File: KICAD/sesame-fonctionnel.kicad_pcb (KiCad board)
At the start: 4 copper layers, 160 x 100 mm, 279 parts, among them J1 CXS70-14-C, J2 CXS70-14-C, J7 CXS70-14-C, J8 CXS70-14-C, J9 Conn_02x16_Odd_Even, Q1 BC847, Q10 BC857, Q11 SQM120, Q12 BC847, Q13 BC847, Q2 BC847, Q3 BC847, Q4 BC847, Q5 BC847, Q6 SQM120, Q7 BC857, Q8 SQM120, Q9 SQM120, U1 AD8030, U10 LT6016, U11 AD8030, U12 UCC27284-Q1, U13 AD8030, U14 AD8030, U15 LT8365, U16 LM4040DBZ-2.5, U17 UCC27284-Q1, U2 LM2903, U3 CD4053BM96, U4 4011, U5 CD4053BM96, U6 CD4053BM96, U7 AD8030, U8 LT6016, U9 AD8030

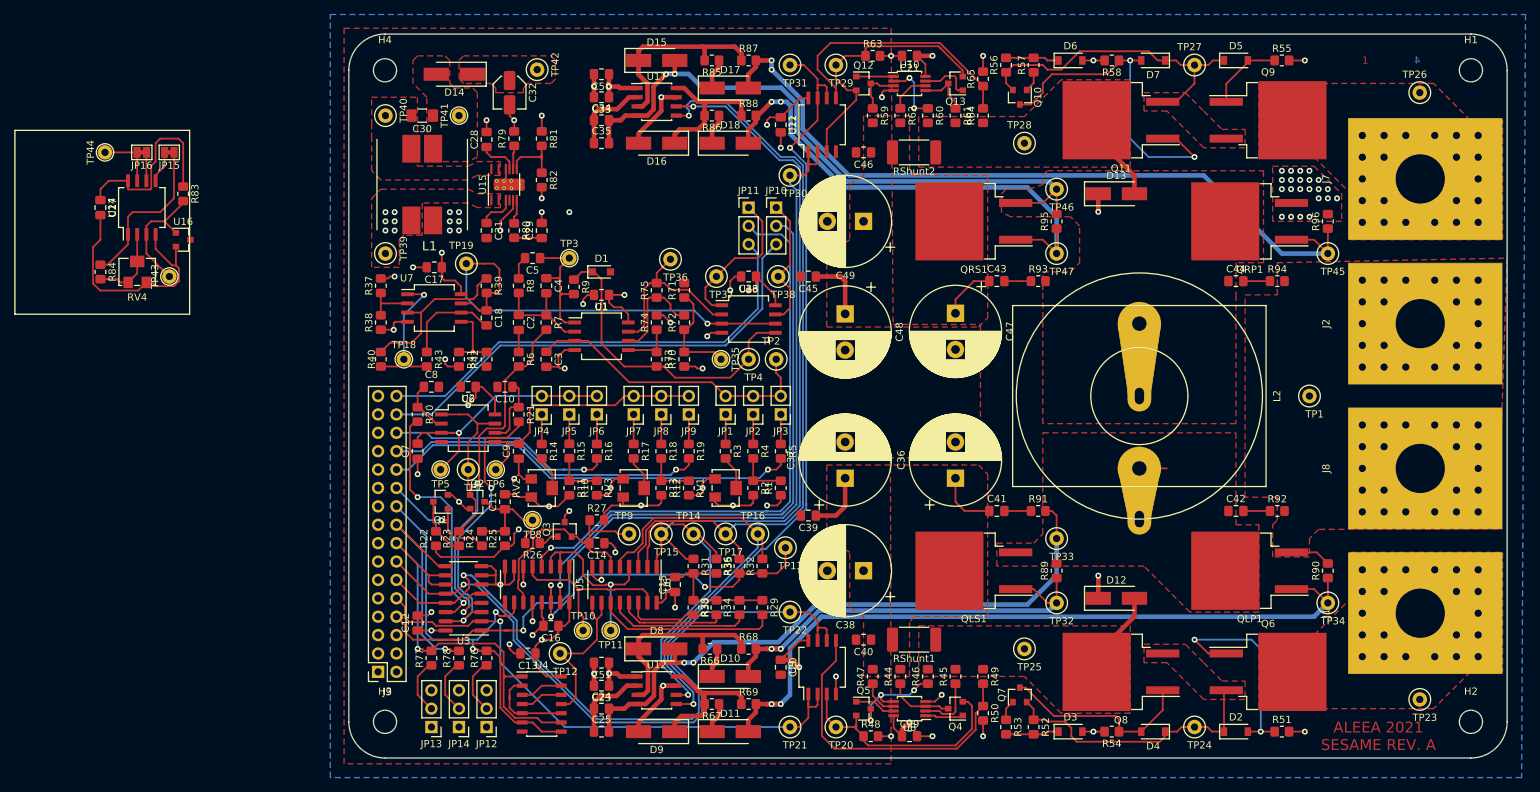
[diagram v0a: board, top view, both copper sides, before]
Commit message: changed ground planes
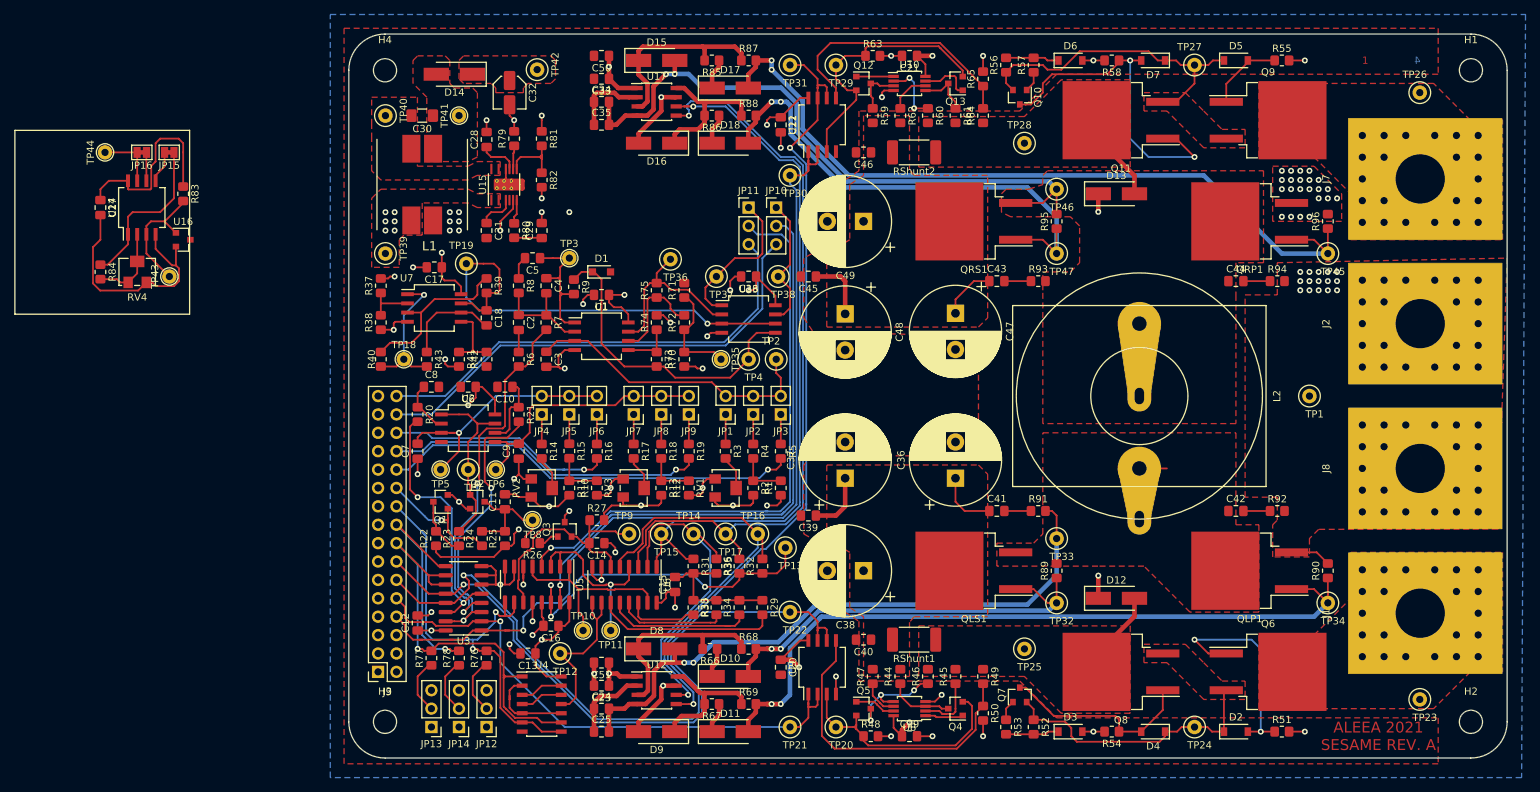
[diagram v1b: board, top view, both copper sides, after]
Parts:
- moved C34 2.54 mm to (114.9, 69.4)
- moved C35 2.54 mm to (114.9, 72.5)
- moved C50 2.54 mm to (114.9, 63.0)
- moved C33 2.54 mm to (114.9, 66.2)
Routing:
- net (no net): track 8.89 -> 0.00 mm
- net GND: track 226.0 -> 222.8 mm, vias 66 -> 80
- net Net-(C34-Pad1): track 11.0 -> 10.4 mm
- added copper zone on In1.Cu, net GND
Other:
- board text added: "Driver Command"

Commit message: enhanced copper planes
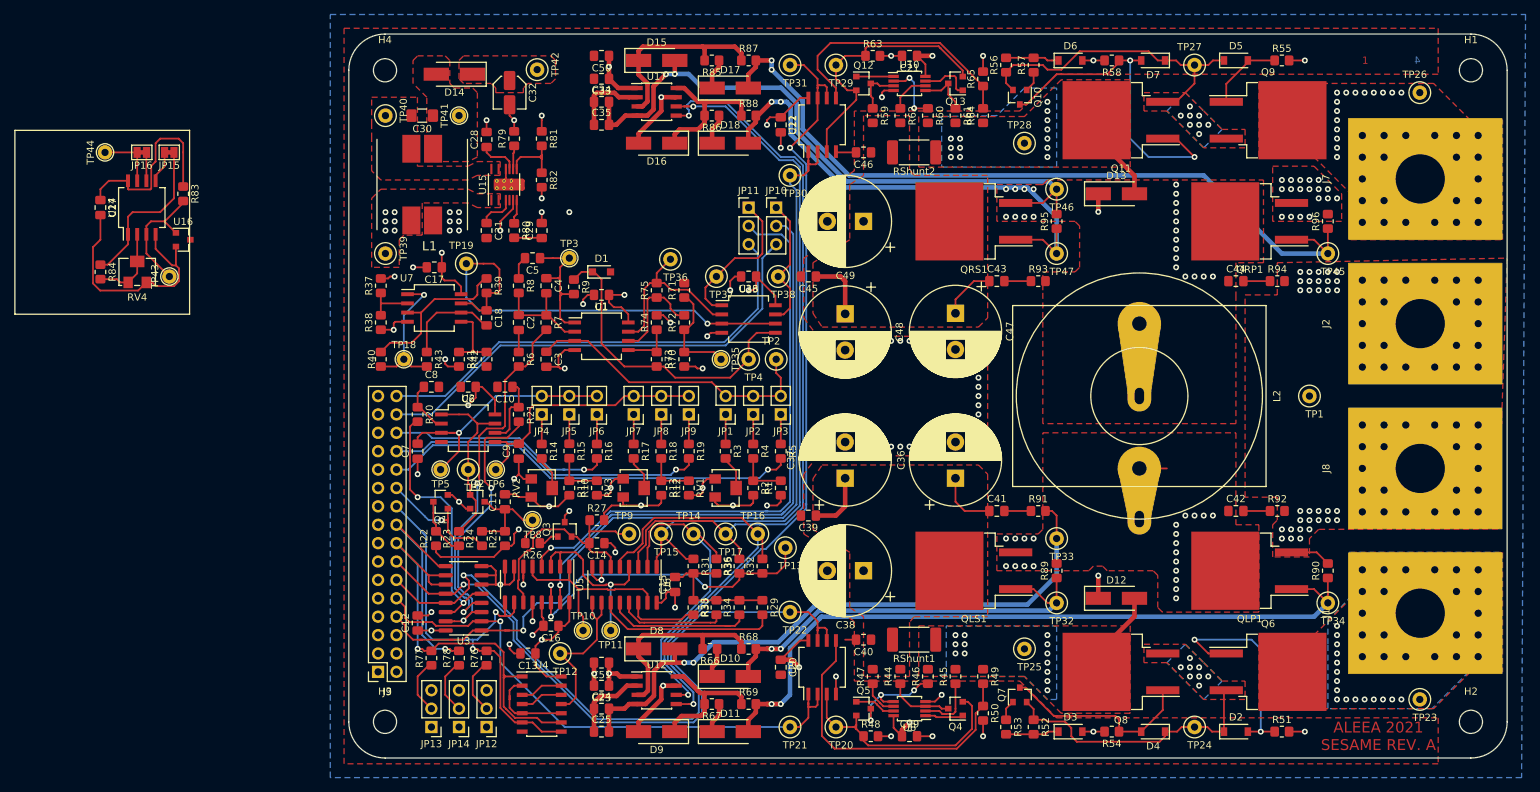
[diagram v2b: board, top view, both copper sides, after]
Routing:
- net GND: track 222.8 -> 227.1 mm, vias 80 -> 122
- net Net-(D7-Pad2): track 46.4 -> 45.6 mm
- net Net-(D5-Pad1): vias 0 -> 8
- net Net-(D2-Pad1): vias 0 -> 8
- net /VProt_Right: vias 0 -> 13
- net /VProt_Left: vias 0 -> 13
- net /R: vias 0 -> 15
- net /MOS DRIVER R/VS: vias 2 -> 21
- net /MOS DRIVER R/VG_P: vias 2 -> 5
- net /MOS DRIVER L/VS: vias 2 -> 23
- net /L: vias 0 -> 16
- added copper zone on B.Cu, net /L
- added copper zone on B.Cu, net /VProt_Left
- added copper zone on B.Cu, net /VProt_Right
- added copper zone on B.Cu, net Net-(D2-Pad1)
- added copper zone on B.Cu, net Net-(D5-Pad1)

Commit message: 0 conn. + new vref
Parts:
- removed JP15, JP16: Jumper_2_Bridged, Jumper:SolderJumper-2_P1.3mm_Bridged_Pad1.0x1.5mm
- removed RV4: 10K, Potentiometer_SMD:Potentiometer_Bourns_3214W_Vertical
- removed TP43, TP44: TP_NOP, TestPoint:TestPoint_THTPad_D2.0mm_Drill1.0mm
- removed U14: AD8030, Package_SO:SO-8_5.3x6.2mm_P1.27mm
- added R28: R, Sesame_footprint:R_0805_2012Metric_Pad1.20x1.40mm_HandSolder, F.Cu at (120.0, 80.2)
- R84: value 10k -> R
- U16: value LM4040DBZ-2.5 -> TL431DBZ
- moved R84 74.7 mm to (120.0, 85.2)
- moved C27 68.1 mm to (113.6, 80.2)
- moved U16 67.6 mm to (124.4, 82.7)
- moved R83 59.7 mm to (116.8, 80.2), turned to 90 degrees
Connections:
- C27 pad 1: VCC -> VREF
- R83 pad 2: Net-(R83-Pad2) -> VREF
- R84 pad 1: VREF -> Net-(R28-Pad2)
- R84 pad 2: Net-(R84-Pad2) -> GND
- U16 pad 1: Net-(R83-Pad2) -> VREF
- U16 pad 2: GND -> Net-(R28-Pad2)
- U16 pad 3: (no net) -> GND
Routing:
- net VCC: track 154.6 -> 129.1 mm, vias 19 -> 20
- net VREF: track 280.7 -> 297.6 mm
- net Net-(R83-Pad2): track 16.3 -> 0.00 mm
- net GND: track 227.1 -> 211.3 mm, vias 122 -> 123
- net Net-(R84-Pad2): track 11.2 -> 0.00 mm
- net Net-(JP16-Pad2): track 8.36 -> 0.00 mm
- net Net-(R28-Pad2): track 0.00 -> 6.77 mm
- net Net-(JP15-Pad2): track 4.43 -> 0.00 mm
- net Net-(JP16-Pad1): track 3.93 -> 0.00 mm
- net /MOS DRIVER R/VS: vias 21 -> 20
- net /MOS DRIVER R/VG_P: vias 5 -> 2

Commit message: mod. ref rail on kicad
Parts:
- R28: value R -> 14k
- R83: value R -> 200
- R84: value R -> 10k

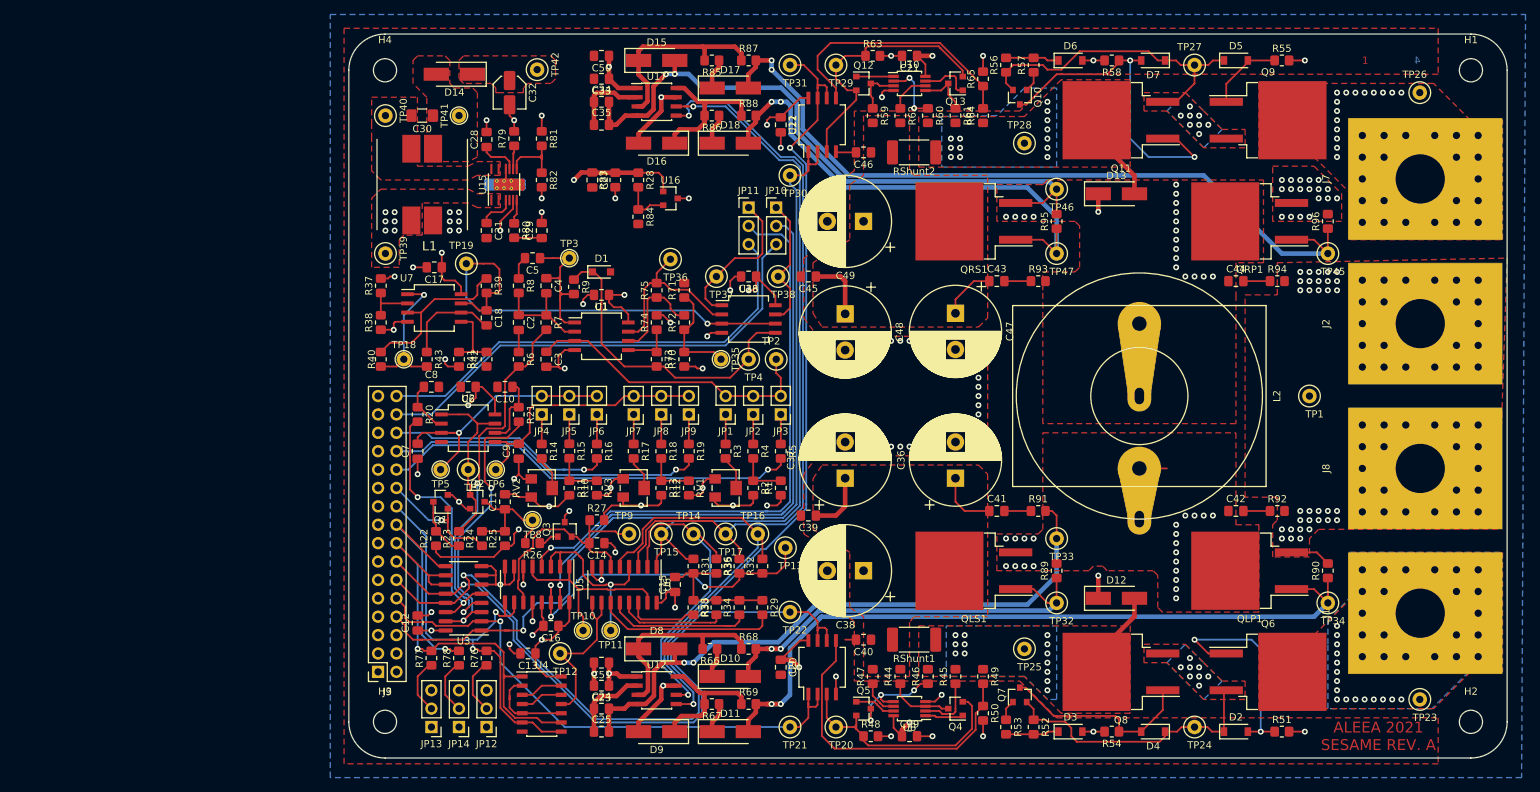
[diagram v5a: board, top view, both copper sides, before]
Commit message: minor changes on the bottom layer + minor silkscreen cleaning
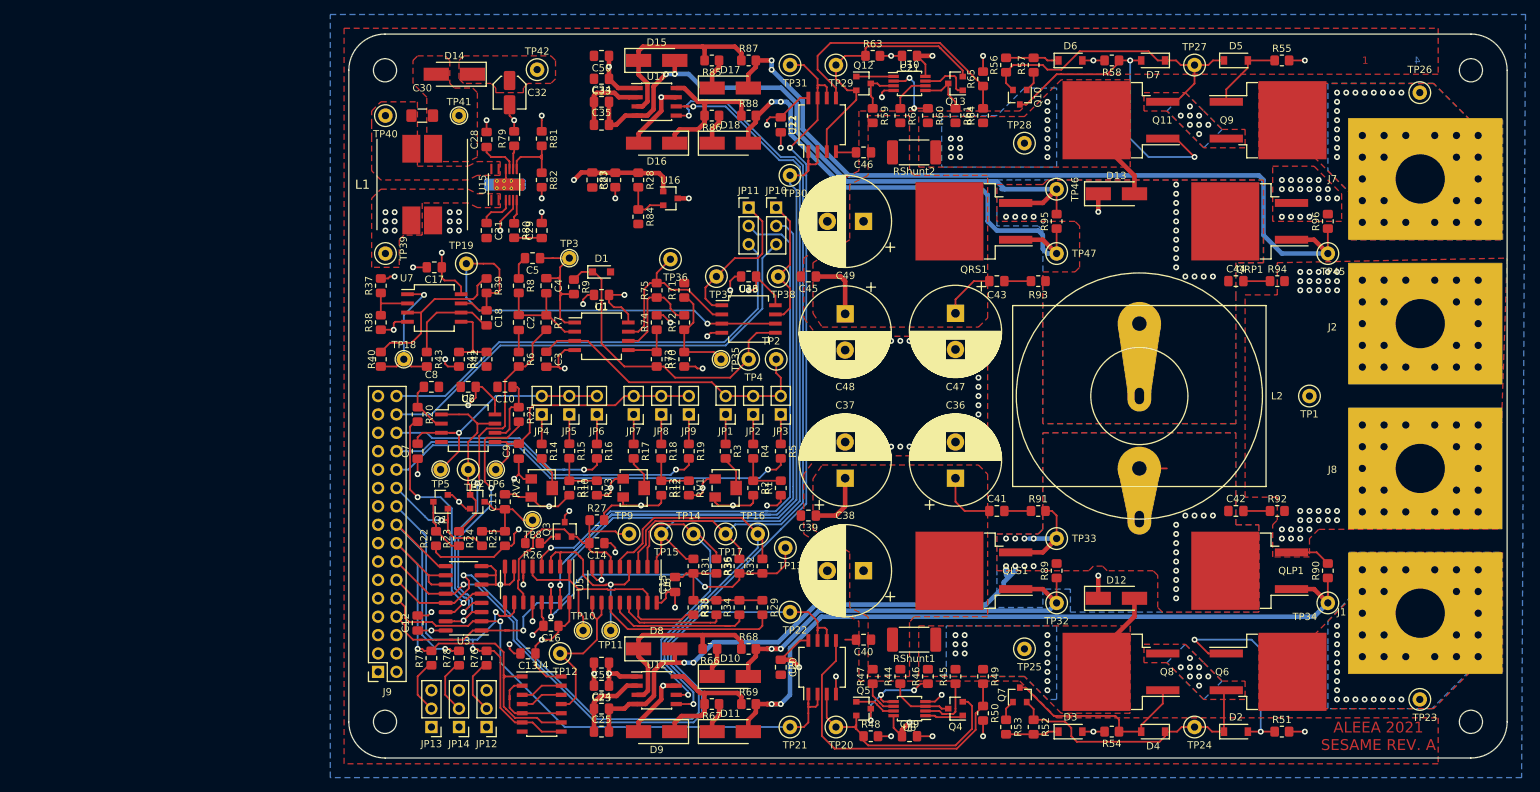
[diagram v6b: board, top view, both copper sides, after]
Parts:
- turned TP41 to 180 degrees
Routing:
- net /PWM: track 81.6 -> 111.6 mm
- net /DC/DC CONVERTER/VG_RP: track 106.6 -> 111.1 mm
- net /MOS DRIVER L/VS: track 92.8 -> 94.8 mm
- net /MOS DRIVER R/VS: track 90.4 -> 91.2 mm
- net /Voltage_Sens_R: track 164.9 -> 164.4 mm
- added copper zone on B.Cu, net /MOS DRIVER L/VS
- added copper zone on B.Cu, net /MOS DRIVER R/VS
- added copper zone on B.Cu, net /R
